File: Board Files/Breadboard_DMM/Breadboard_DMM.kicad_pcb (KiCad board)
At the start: 4 copper layers, 89.3 x 90.7 mm, 146 parts, among them J101 Conn_02x05_Odd_Even, J102 Conn_02x05_Odd_Even, J301 V+, J302 I+, J701 Conn_01x06, J702 AudioJack3, J703 Conn_02x02_Top_Bottom, K301 EC2-5NU, K302 EC2-5NU, K501 EC2-5NU, Q201 BSD840N, Q301 BSD840N, Q401 BSD840N, Q402 BSD840N, Q501 BSD840N, Q502 BSD840N, Q701 BSD840N, Q801 DMP3085LSD, Q802 PMBT2907A, SW101 L102021ML04Q, SW701 SW_Push, SW702 SW_Push, SW703 SW_Push, SW704 SW_Push, SW705 SW_Push, U101 MIC5365-3.3YD5, U201 NAU7802, U202 MAX6070x41, U301 LMV358, U401 LMV358, U402 MCP1501, U501 74VHC4052AFT, U701 SI8422, U702 LCD-Generic_3.2in_SPI_SD, U703 STM32G030Kx, U801 TL432LI

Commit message: 59 unrouted nodes
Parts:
- C401, C402, C403, D301, D401, Q401, R401, R402, R403, R404, R405, U401, U402: moved to F.Cu
- TP701, TP702: footprint TestPoint:TestPoint_THTPad_D2.5mm_Drill1.2mm -> TestPoint:TestPoint_THTPad_D1.5mm_Drill0.7mm
- moved R711 88.9 mm to (104.5, 106.9)
- moved D101 28.6 mm to (180.8, 66.2), turned to 180 degrees
- moved U702 26.7 mm to (90.2, -23.5)
- moved R101 26.0 mm to (179.1, 63.4), turned to 180 degrees
- moved C402 22.7 mm to (138.9, 96.4), turned to 90 degrees
- moved U401 15.6 mm to (143.9, 95.8), turned to 180 degrees
- moved C401 13.4 mm to (140.7, 90.7), turned to 90 degrees
- moved R410 12.4 mm to (164.7, 98.3), turned to 90 degrees
- moved R403 12.4 mm to (150.9, 98.6), turned to 90 degrees
- moved R404 12.2 mm to (151.8, 95.8), turned to 0 degrees
- moved Q401 11.5 mm to (153.5, 92.3), turned to 270 degrees
- moved R405 11.4 mm to (150.9, 92.8), turned to 90 degrees
- moved D401 11.3 mm to (154.1, 97.9), turned to 0 degrees
- moved C403 11.2 mm to (149.0, 96.8), turned to 90 degrees
- moved U402 10.3 mm to (143.9, 90.7), turned to 180 degrees
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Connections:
- U703 pad 7: /ADC/VREF_4.096V_~EN -> /ADC/ADC_~DRDY
- U703 pad 8: /ADC/ADC_~DRDY -> /ADC/VREF_4.096V_~EN
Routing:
- net GNDL: track 17.6 -> 160.6 mm, vias 0 -> 3
- net Net-(J101-Pad10): track 0.00 -> 105.3 mm
- net /ADC/I_SENSE-: track 9.39 -> 104.9 mm
- net GND: track 17.3 -> 99.0 mm, vias 0 -> 47
- net /MCU & Display/MCU_PROG_RX: track 0.00 -> 76.2 mm, vias 0 -> 1
- net /MCU & Display/MCU_PROG_TX: track 0.00 -> 75.2 mm, vias 0 -> 1
- net /Front End/METER_CURRENT_SOURCE_ON: track 0.00 -> 70.8 mm, vias 0 -> 2
- net /MCU & Display/MCU_TX: track 0.00 -> 61.8 mm, vias 0 -> 2
- net /MCU & Display/MCU_RX: track 0.00 -> 61.4 mm, vias 0 -> 2
- net /Front End/SET_CURRENT_SOURCE_B: track 0.00 -> 61.3 mm, vias 0 -> 2
- net /Front End/CALIBRATE_RELAY_ON: track 0.00 -> 60.4 mm, vias 0 -> 2
- net /Front End/CALIBRATE_MUX_~B: track 0.00 -> 59.2 mm, vias 0 -> 2
- net /Front End/SET_CURRENT_SOURCE_A: track 0.00 -> 55.4 mm, vias 0 -> 2
- net /Front End/CALIBRATE_MUX_~A: track 0.00 -> 52.2 mm, vias 0 -> 2
- net /MCU & Display/MCU_NRST: track 4.28 -> 48.8 mm, vias 0 -> 2
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- added copper zone on F.Cu, net +3V3
- added copper zone on In2.Cu, net +5VA
- added copper zone on In1.Cu, net GND

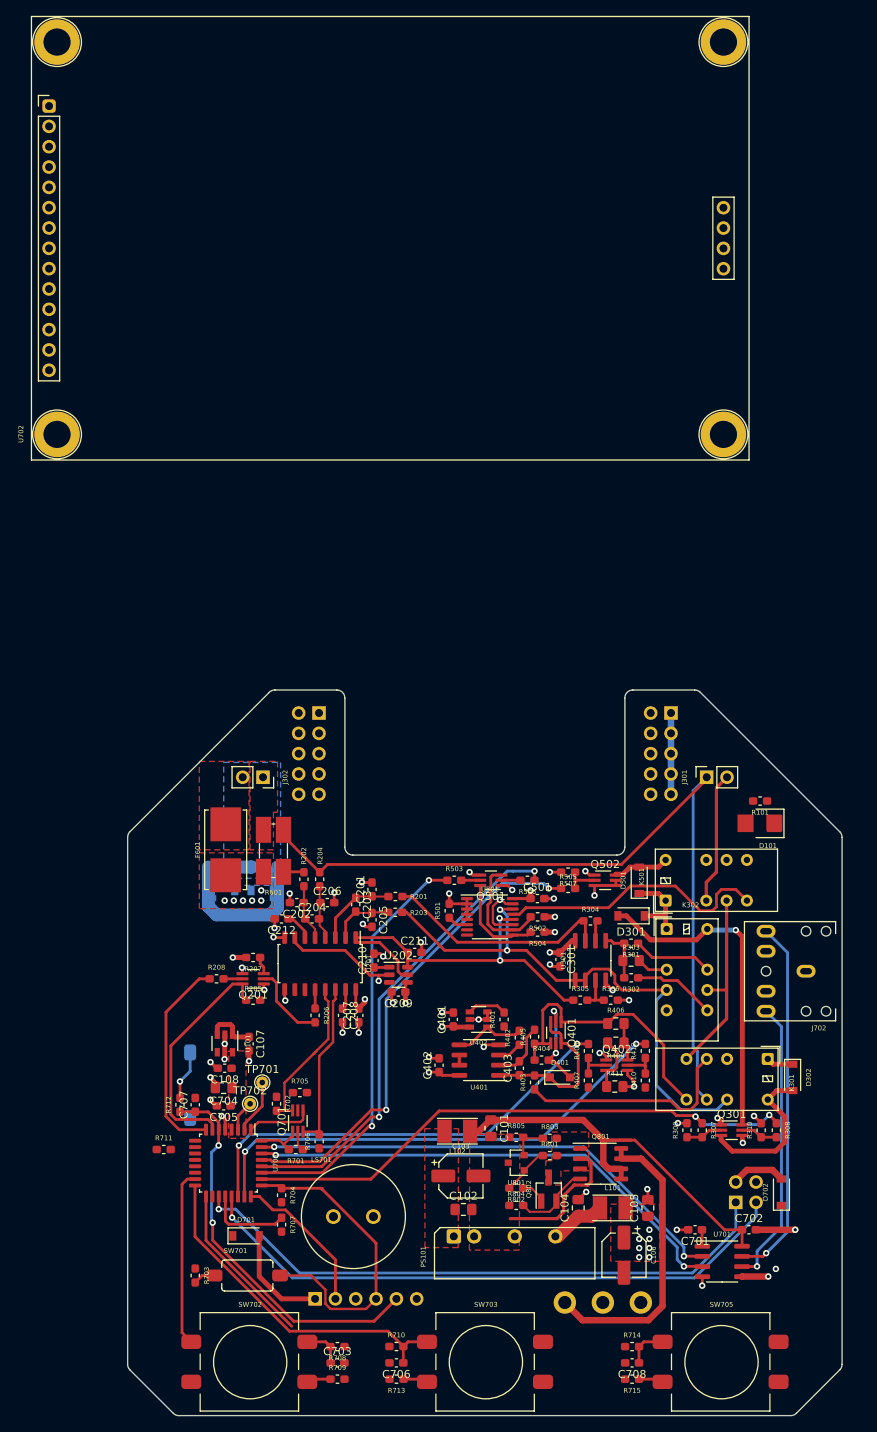
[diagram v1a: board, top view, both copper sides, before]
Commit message: Added silkscreen graphics and BOM
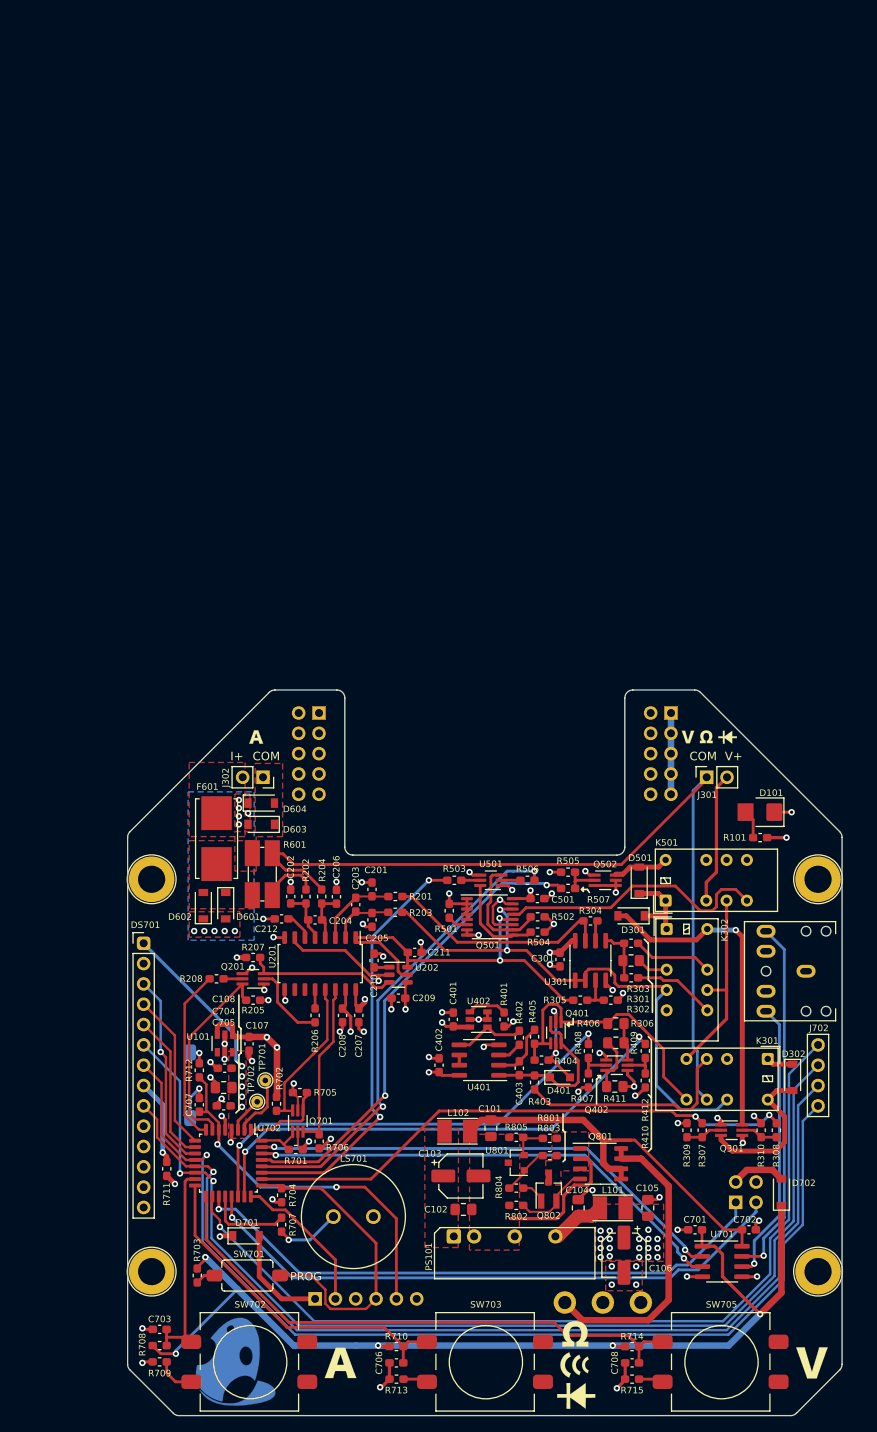
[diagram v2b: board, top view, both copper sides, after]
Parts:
- removed the U702 at (90.2, -23.5)
- added DS701: LCD-Generic_3.2in_SPI_SD, irex_Display:LCD-Generic-3.2in_89.30x55.04mm_ReducedCourtyard, F.Cu at (102.0, 81.2)
- added G***: LOGO, Breadboard_DMM_Aesthetic:input_amps, F.Cu at (116.1, 55.4)
- added G***: LOGO, Breadboard_DMM_Aesthetic:input_v, F.Cu at (172.7, 55.4)
- added G***: IREX_LOGO, irex_Aesthetic:Logo_irex_10.0x11.1mm_Copper, B.Cu at (113.5, 133.5)
- added G***: LOGO, Breadboard_DMM_Aesthetic:ohms_cont_diode, F.Cu at (156.1, 133.9)
- added G***: LOGO, Breadboard_DMM_Aesthetic:volt, F.Cu at (185.5, 133.6)
- added G***: LOGO, Breadboard_DMM_Aesthetic:amp, F.Cu at (126.6, 133.6)
- D601, D602, D603, D604: moved to F.Cu
- moved C703 22.6 mm to (104.0, 129.4), turned to 180 degrees
- moved R709 22.3 mm to (104.0, 133.5), turned to 180 degrees
- moved R708 22.2 mm to (104.0, 131.4), turned to 0 degrees
- moved D604 9.41 mm to (116.7, 63.6)
- moved D603 5.35 mm to (116.7, 66.3), turned to 180 degrees
- moved D601 5.19 mm to (112.3, 76.5), turned to 270 degrees
- moved R712 4.95 mm to (109.0, 97.0)
- moved R101 4.57 mm to (179.1, 67.9)
- moved R601 3.24 mm to (116.8, 72.5)
- moved D602 2.98 mm to (109.5, 76.5), turned to 90 degrees
- moved R711 2.44 mm to (104.9, 109.3), turned to 270 degrees
- moved R202 2.17 mm to (122.3, 75.3)
- moved R204 2.17 mm to (124.3, 75.3)
- moved F601 1.81 mm to (111.1, 68.1)
- moved D101 1.40 mm to (180.8, 64.8)
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- renumbered U703 to U702
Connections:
- R101 pad 1: +5VD -> +5VA
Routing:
- net +3V3: track 4.51 -> 211.8 mm, vias 0 -> 15
- net /MCU & Display/SPI_MOSI: track 0.00 -> 135.9 mm, vias 0 -> 2
- net /MCU & Display/SPI_SCK: track 0.00 -> 131.8 mm, vias 0 -> 1
- net /MCU & Display/SPI_MISO: track 0.00 -> 127.3 mm, vias 0 -> 1
- net /MCU & Display/SPI_SD_CS: track 0.00 -> 111.5 mm, vias 0 -> 1
- net +5VD: track 15.9 -> 100.5 mm, vias 0 -> 5
- net /MCU & Display/BTN3: track 25.9 -> 70.3 mm
- net /MCU & Display/SPI_LCD_CS: track 0.00 -> 24.5 mm, vias 0 -> 1
- net GND: track 99.0 -> 122.0 mm, vias 47 -> 59
- net /MCU & Display/LCD_~RESET~: track 0.00 -> 19.7 mm
- net Net-(D601-Pad2): track 19.5 -> 0.00 mm, vias 0 -> 10
- net /MCU & Display/LCD_DC: track 0.00 -> 18.7 mm
- net Net-(Q201-Pad3): track 2.31 -> 19.0 mm
- net Net-(DS701-Pad8): track 0.00 -> 10.7 mm, vias 0 -> 1
- net Net-(LS701-Pad1): track 0.00 -> 8.20 mm, vias 0 -> 1
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- added copper zone on F.Cu, net GND
- added copper zone on B.Cu, net Net-(D601-Pad2)
- added copper zone on F.Cu, net Net-(D601-Pad2)
- removed copper zone on B.Cu, net /ADC/I_SENSE+
- removed copper zone on B.Cu, net /ADC/I_SENSE-
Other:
- board text added: "COM"
- board text added: "I+"
- board text added: "PROG"
- board text added: "Reset"
- board text added: "Rev 0 I. Rex"
- board text added: "SWD Programming"
- board text added: "Toast-O-Meter"
- board text added: "UART Debug"
- board text added: "V+"
